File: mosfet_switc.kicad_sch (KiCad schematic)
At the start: 10 parts, among them J12 Thrusters, J4 Raspberry Pi / Camera, J7 Sensors / Control board

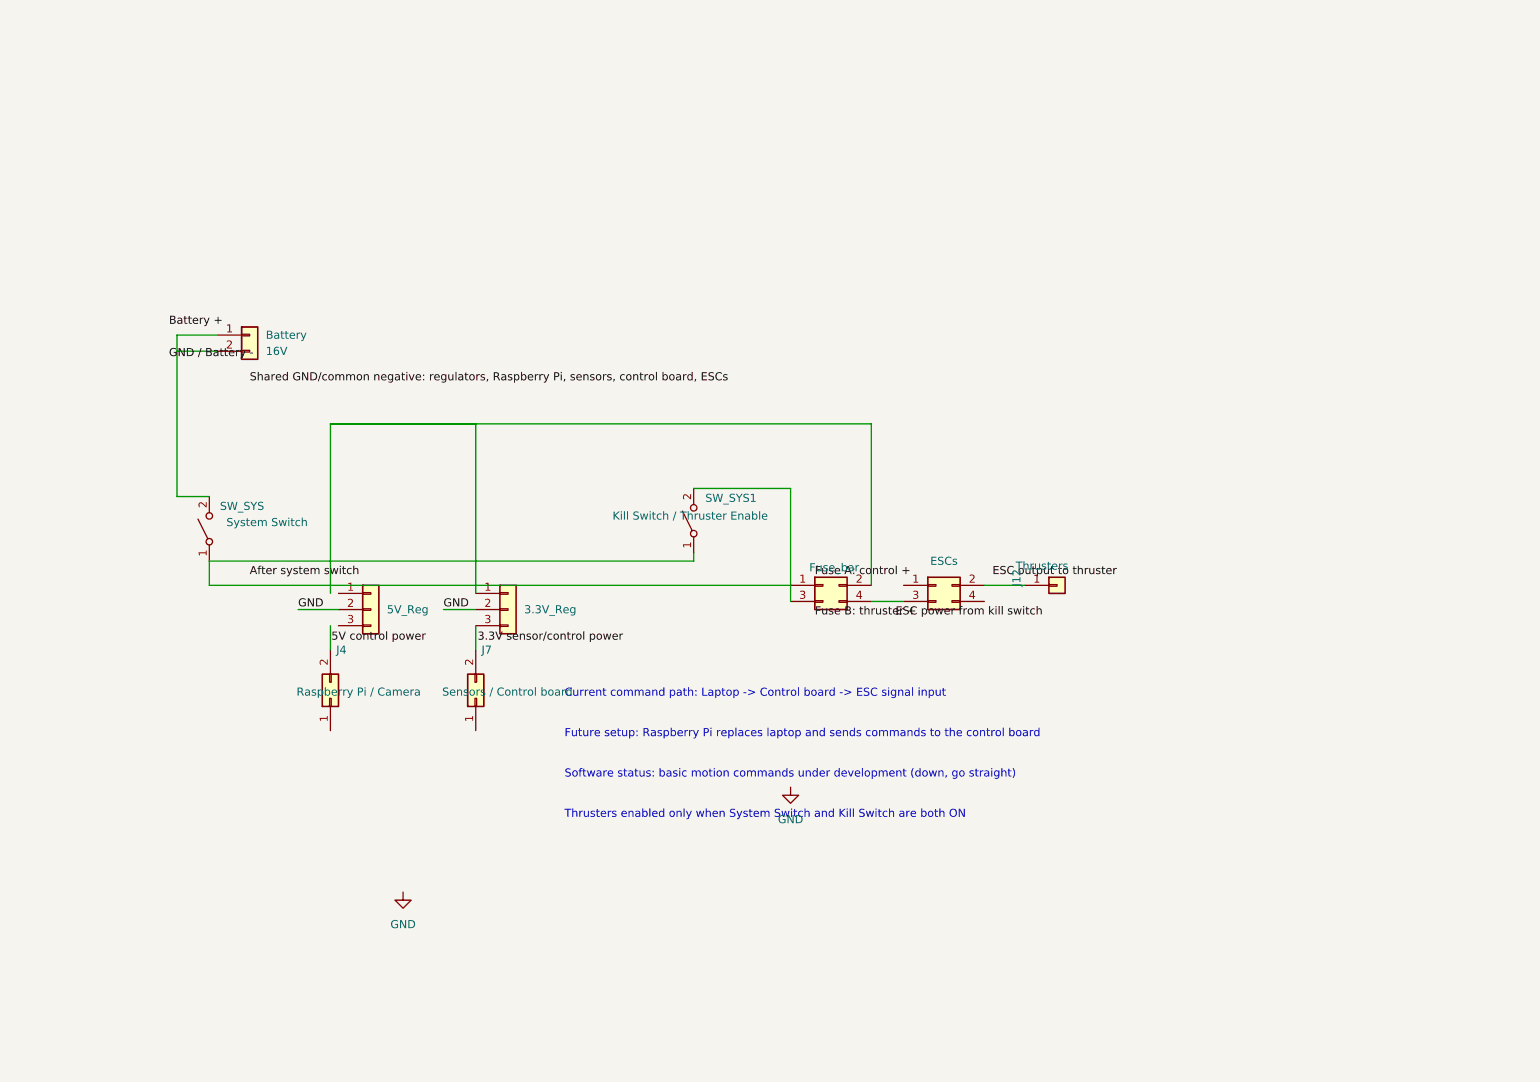
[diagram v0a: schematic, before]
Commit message: Add MOSFET gate drive detail
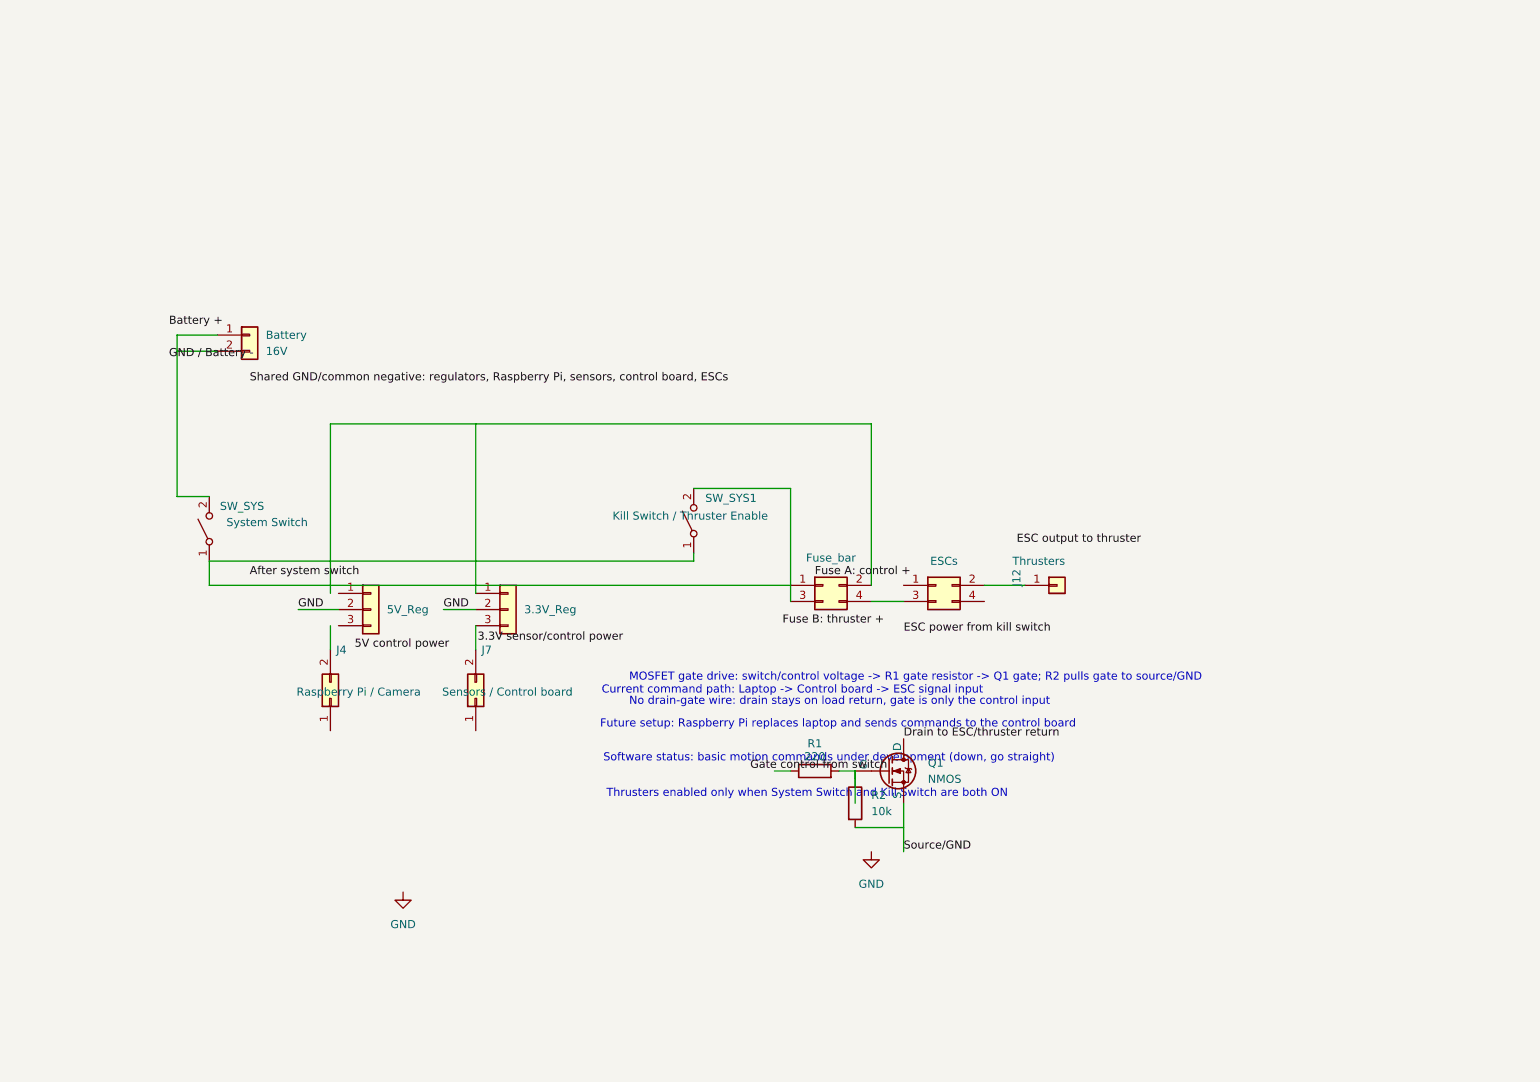
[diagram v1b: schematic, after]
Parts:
- added Q1: NMOS, symbol Simulation_SPICE:NMOS
- added R1: 220, symbol Device:R
- added R2: 10k, symbol Device:R
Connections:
- net at Fuse_bar.2 (Pin_2): no longer 3.3V_Reg.1 (Pin_1)
- new net: Q1.2 (G), R1.2, R2.1
- new net Drain to ESC/thruster return: Q1.1 (D)
- new net Source/GND: Q1.3 (S)
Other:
- note added: "MOSFET gate drive: switch/control voltage -> R1 gate resistor -> Q1 gate; R2 pulls gate to source/GND"
- note added: "No drain-gate wire: drain stays on load return, gate is only the control input"

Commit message: Create text-box power system layout
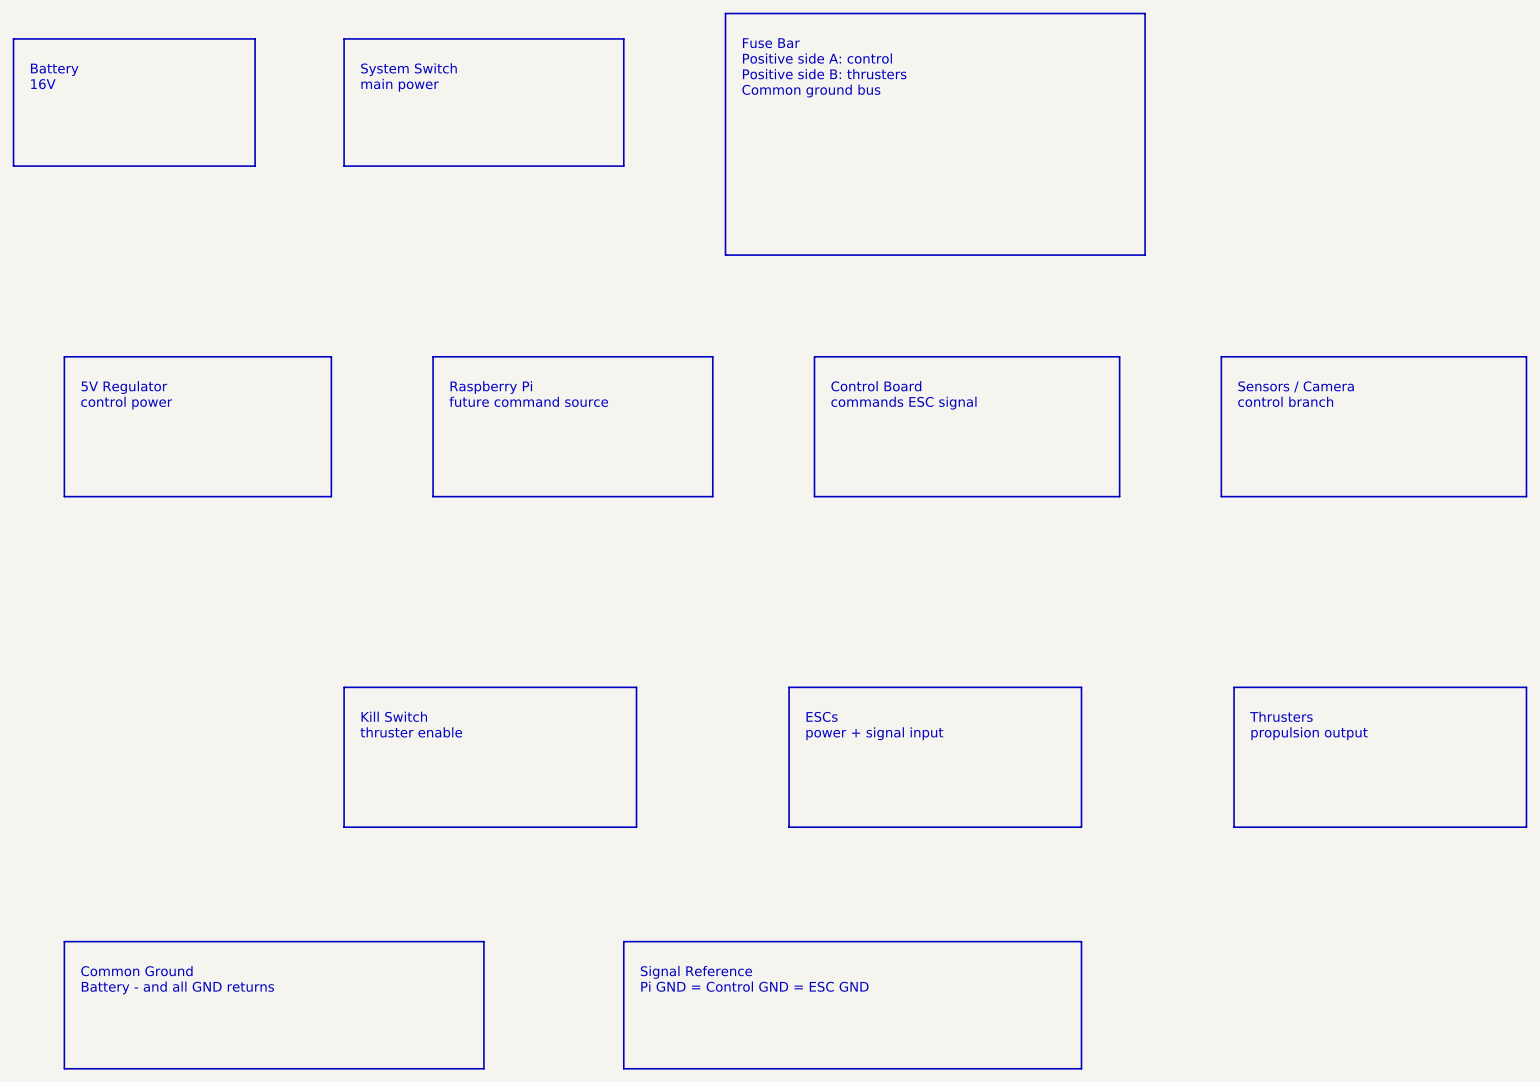
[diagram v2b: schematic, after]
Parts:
- removed 3.3V_Reg, 5V_Reg: Conn_01x03, symbol Connector_Generic:Conn_01x03
- removed Battery: 16V, symbol Connector_Generic:Conn_01x02
- removed ESCs, Fuse_bar: Conn_02x02_Odd_Even, symbol Connector_Generic:Conn_02x02_Odd_Even
- removed J12: Thrusters, symbol Connector_Generic:Conn_01x01
- removed J4: Raspberry Pi / Camera, symbol Connector_Generic:Conn_02x01
- removed J7: Sensors / Control board, symbol Connector_Generic:Conn_02x01
- removed Q1: NMOS, symbol Simulation_SPICE:NMOS
- removed R1: 220, symbol Device:R
- removed R2: 10k, symbol Device:R
- removed SW_SYS: System Switch, symbol Switch:SW_SPST
- removed SW_SYS1: Kill Switch / Thruster Enable, symbol Switch:SW_SPST
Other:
- note added: "5V Regulator control power"
- note added: "Battery 16V"
- note added: "Common Ground Battery - and all GND returns"
- note added: "Control Board commands ESC signal"
- note added: "ESCs power + signal input"
- note added: "Fuse Bar Positive side A: control Positive side B: thrusters Common ground bus"
- note added: "Kill Switch thruster enable"
- note added: "Raspberry Pi future command source"
- note added: "Sensors / Camera control branch"
- note added: "Signal Reference Pi GND = Control GND = ESC GND"
- note added: "System Switch main power"
- note added: "Thrusters propulsion output"
- note removed: "Current command path: Laptop -> Control board -> ESC signal input"
- note removed: "Future setup: Raspberry Pi replaces laptop and sends commands to the control board"
- note removed: "MOSFET gate drive: switch/control voltage -> R1 gate resistor -> Q1 gate; R2 pulls gate to source/GND"
- note removed: "No drain-gate wire: drain stays on load return, gate is only the control input"
- note removed: "Software status: basic motion commands under development (down, go straight)"
- note removed: "Thrusters enabled only when System Switch and Kill Switch are both ON"
